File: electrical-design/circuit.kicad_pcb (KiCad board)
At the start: 4 copper layers, 90 x 70 mm, 49 parts, among them J1 AVR-ISP-10, J2 Analoge Header, Q1 2N3906, Q2 2N3906, Q3 2N3906, Q4 2N3906, SW1 Reset Button, SW2 SW_DIP_x04, SW3 Reset Button, U1 ATmega8A-P, U2 LTC-4627JD, U3 NE555P, Y1 16MHz

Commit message: Completed Design For Rev 1.0
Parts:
- removed kibuzzard-63E778F7: G***, kibuzzard-63E778F7
- added C7: 33uF, Capacitor_THT:CP_Radial_D4.0mm_P1.50mm, F.Cu at (129.0, 63.5)
- moved R2 14.7 mm to (122.4, 83.6)
- moved R3 7.78 mm to (122.4, 81.0)
- moved D1 1.27 mm to (136.9, 82.5)
- moved D2 1.27 mm to (128.5, 82.5)
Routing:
- net Net-(D1-K): track 4.57 -> 15.7 mm
- net Net-(D2-K): track 4.58 -> 6.73 mm
- net Net-(D2-A): track 9.27 -> 10.5 mm
- net Net-(D1-A): track 17.8 -> 19.1 mm
- net Net-(U2-DP): track 49.6 -> 49.1 mm
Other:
- board text added: "ATMEGA8A Evaluation Board"
- board text added: "Rev 1.0"

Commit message: Created Parts Order List And Modified PCB Rev 1.0 Accordingly
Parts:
- removed J2: Analoge Header, Connector_JST:JST_XH_B3B-XH-A_1x03_P2.50mm_Vertical
- added TP1: TP Ground, TestPoint:TestPoint_THTPad_2.0x2.0mm_Drill1.0mm, F.Cu at (103.6, 86.4)
- added TP2: TP Frequency, TestPoint:TestPoint_THTPad_2.0x2.0mm_Drill1.0mm, F.Cu at (109.7, 86.4)
- added VR1: PTV09A-4015F-B503, Potentiometer:PTV09A4020FB103, F.Cu at (137.1, 38.6)
- C7: footprint Capacitor_THT:CP_Radial_D4.0mm_P1.50mm -> Capacitor_THT:CP_Radial_D4.0mm_P2.00mm
- SW2: value SW_DIP_x04 -> DS02C-254-1L-04BE; footprint Button_Switch_THT:SW_DIP_SPSTx04_Slide_9.78x12.34mm_W7.62mm_P2.54mm -> DIP Switch:DS02C2541L04BE
- U2: value LTC-4627JD -> LTC-4627JR; footprint Display_7Segment:LTC-4627Jx -> 7 Segment Display:DIPS1016W50P254L4018H725Q16N
- moved R15 18.3 mm to (84.3, 87.4), turned to 180 degrees
- moved R14 15.7 mm to (84.3, 84.8), turned to 180 degrees
- moved R13 13.5 mm to (84.3, 82.3), turned to 180 degrees
- moved R12 12.1 mm to (84.3, 79.8), turned to 180 degrees
- moved SW2 10.8 mm to (66.3, 76.4), turned to 0 degrees
- moved J1 2.02 mm to (136.8, 55.9)
- moved C7 0.22 mm to (128.8, 63.5)
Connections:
- R12 pad 2: Net-(R12-Pad2) -> Net-(SW2-COM4)
- R13 pad 2: Net-(R13-Pad2) -> Net-(SW2-COM3)
- R14 pad 2: Net-(R14-Pad2) -> Net-(SW2-COM2)
- R15 pad 2: Net-(R15-Pad2) -> Net-(SW2-COM1)
- R16 pad 2: Net-(U3-DIS) -> Net-(SW2-NO1)
- R17 pad 1: Net-(U3-DIS) -> Net-(SW2-NO1)
- SW2 pad 1: Net-(U3-DIS) -> Net-(SW2-COM1)
- SW2 pad 2: Net-(U3-DIS) -> Net-(SW2-COM2)
- SW2 pad 3: Net-(U3-DIS) -> Net-(SW2-COM3)
- SW2 pad 4: Net-(U3-DIS) -> Net-(SW2-COM4)
- SW2 pad 5: Net-(R15-Pad2) -> Net-(SW2-NO1)
- SW2 pad 6: Net-(R14-Pad2) -> Net-(SW2-NO1)
- SW2 pad 7: Net-(R13-Pad2) -> Net-(SW2-NO1)
- SW2 pad 8: Net-(R12-Pad2) -> Net-(SW2-NO1)
- U3 pad 7: Net-(U3-DIS) -> Net-(SW2-NO1)
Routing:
- net Net-(U3-DIS): track 35.7 -> 0.00 mm
- net Net-(SW2-NO1): track 0.00 -> 35.7 mm
- net Net-(SW2-COM1): track 0.00 -> 17.5 mm
- net Net-(SW2-COM2): track 0.00 -> 13.9 mm
- net Net-(SW2-COM3): track 0.00 -> 10.3 mm
- net Net-(SW2-COM4): track 0.00 -> 6.73 mm
- net Net-(R15-Pad2): track 4.25 -> 0.00 mm
- net Net-(R14-Pad2): track 4.25 -> 0.00 mm
- net Net-(R13-Pad2): track 4.25 -> 0.00 mm
- net Net-(R12-Pad2): track 4.25 -> 0.00 mm
- net Net-(U1-PC4): track 16.7 -> 20.3 mm
- net Frequency: track 42.9 -> 46.1 mm
- net ~{RESET}: track 43.5 -> 46.3 mm
- net MISO: track 13.3 -> 12.4 mm
- net SCK: track 13.3 -> 12.4 mm

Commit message: Send R1.0 to Production
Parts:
- added R24: 1K, Resistor_THT:R_Axial_DIN0204_L3.6mm_D1.6mm_P5.08mm_Horizontal, F.Cu at (128.3, 47.8)
- added R25: 1K, Resistor_THT:R_Axial_DIN0204_L3.6mm_D1.6mm_P5.08mm_Horizontal, F.Cu at (128.3, 29.5)
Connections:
- VR1 pad 1: VCC -> Net-(R24-Pad2)
- VR1 pad 3: GND -> Net-(R25-Pad2)
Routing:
- net Net-(R24-Pad2): track 0.00 -> 13.0 mm
- net Net-(R25-Pad2): track 0.00 -> 13.0 mm
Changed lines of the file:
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@@
   (net 58 "Net-(SW2-COM3)")
   (net 59 "Net-(SW2-COM4)")
+  (net 60 "Net-(R25-Pad2)")
+  (net 61 "Net-(R24-Pad2)")
   (footprint "Button_Switch_THT:SW_PUSH_6mm_H5mm" (layer "F.Cu")
     (at 88.19 81.062)
@@
     )
   )
+  (footprint "Resistor_THT:R_Axial_DIN0204_L3.6mm_D1.6mm_P5.08mm_Horizontal" (layer "F.Cu")
+    (at 128.27 29.464)
+    (descr "Resistor, Axial_DIN0204 series, Axial, Horizontal, pin pitch=5.08mm, 0.167W, length*diameter=3.6*1.6mm^2, http://cdn-reichelt.de/documents/datenblatt/B400/1_4W%23YAG.pdf")
+    (tags "Resistor Axial_DIN0204 series Axial Horizontal pin pitch 5.08mm 0.167W length 3.6mm diameter 1.6mm")
+    (property "Sheetfile" "circuit.kicad_sch")
+    (property "Sheetname" "")
+    (property "ki_description" "Resistor, small symbol")
+    (property "ki_keywords" "R resistor")
+    (attr through_hole)
+    (fp_text reference "R25" (at 2.54 -1.92) (layer "F.SilkS")
+        (effects (font (size 0.75 0.75) (thickness 0.1)))
+    )
+    (fp_text value "1K" (at 2.54 1.92 unlocked) (layer "F.Fab")
+        (effects (font (size 1 1) (thickness 0.15)))
+    )
+    (fp_text user "${REFERENCE}" (at 2.54 0 unlocked) (layer "F.Fab")
+        (effects (font (size 1 1) (thickness 0.15)))
+    )
+    (fp_line (start 0.62 -0.92) (end 4.46 -0.92)
+      (stroke (width 0.1) (type solid)) (layer "F.SilkS"))
+    (fp_line (start 0.62 0.92) (end 4.46 0.92)
+      (stroke (width 0.1) (type solid)) (layer "F.SilkS"))
+    (fp_line (start -0.95 -1.05) (end -0.95 1.05)
+      (stroke (width 0.05) (type solid)) (layer "F.CrtYd"))
+    (fp_line (start -0.95 1.05) (end 6.03 1.05)
+      (stroke (width 0.05) (type solid)) (layer "F.CrtYd"))
+    (fp_line (start 6.03 -1.05) (end -0.95 -1.05)
+      (stroke (width 0.05) (type solid)) (layer "F.CrtYd"))
+    (fp_line (start 6.03 1.05) (end 6.03 -1.05)
+      (stroke (width 0.05) (type solid)) (layer "F.CrtYd"))
+    (fp_line (start 0 0) (end 0.74 0)
+      (stroke (width 0.1) (type solid)) (layer "F.Fab"))
+    (fp_line (start 0.74 -0.8) (end 0.74 0.8)
+      (stroke (width 0.1) (type solid)) (layer "F.Fab"))
+    (fp_line (start 0.74 0.8) (end 4.34 0.8)
+      (stroke (width 0.1) (type solid)) (layer "F.Fab"))
+    (fp_line (start 4.34 -0.8) (end 0.74 -0.8)
+      (stroke (width 0.1) (type solid)) (layer "F.Fab"))
+    (fp_line (start 4.34 0.8) (end 4.34 -0.8)
+      (stroke (width 0.1) (type solid)) (layer "F.Fab"))
+    (fp_line (start 5.08 0) (end 4.34 0)
+      (stroke (width 0.1) (type solid)) (layer "F.Fab"))
+    (pad "1" thru_hole circle (at 0 0) (size 1.4 1.4) (drill 0.7) (layers "*.Cu" "*.Mask")
+      (net 13 "GND") (pintype "passive"))
+    (pad "2" thru_hole oval (at 5.08 0) (size 1.4 1.4) (drill 0.7) (layers "*.Cu" "*.Mask")
+      (net 60 "Net-(R25-Pad2)") (pintype "passive"))
+    (model "${KICAD6_3DMODEL_DIR}/Resistor_THT.3dshapes/R_Axial_DIN0204_L3.6mm_D1.6mm_P5.08mm_Horizontal.wrl"
+      (offset (xyz 0 0 0))
+      (scale (xyz 1 1 1))
+      (rotate (xyz 0 0 0))
+    )
+  )
   (footprint "MountingHole:MountingHole_2.2mm_M2_DIN965_Pad_TopBottom" (layer "F.Cu")
     (at 142.96 27.94)
@@
   )
   (footprint "Resistor_THT:R_Axial_DIN0204_L3.6mm_D1.6mm_P5.08mm_Horizontal" (layer "F.Cu")
+    (at 128.27 47.752)
+    (descr "Resistor, Axial_DIN0204 series, Axial, Horizontal, pin pitch=5.08mm, 0.167W, length*diameter=3.6*1.6mm^2, http://cdn-reichelt.de/documents/datenblatt/B400/1_4W%23YAG.pdf")
+    (tags "Resistor Axial_DIN0204 series Axial Horizontal pin pitch 5.08mm 0.167W length 3.6mm diameter 1.6mm")
+    (property "Sheetfile" "circuit.kicad_sch")
+    (property "Sheetname" "")
+    (property "ki_description" "Resistor, small symbol")
+    (property "ki_keywords" "R resistor")
+    (attr through_hole)
+    (fp_text reference "R24" (at 2.54 -1.92) (layer "F.SilkS")
+        (effects (font (size 0.75 0.75) (thickness 0.1)))
+    )
+    (fp_text value "1K" (at 2.54 1.92 180 unlocked) (layer "F.Fab")
+        (effects (font (size 1 1) (thickness 0.15)))
+    )
+    (fp_text user "${REFERENCE}" (at 2.54 0 180 unlocked) (layer "F.Fab")
+        (effects (font (size 1 1) (thickness 0.15)))
+    )
+    (fp_line (start 0.62 -0.92) (end 4.46 -0.92)
+      (stroke (width 0.1) (type solid)) (layer "F.SilkS"))
+    (fp_line (start 0.62 0.92) (end 4.46 0.92)
+      (stroke (width 0.1) (type solid)) (layer "F.SilkS"))
+    (fp_line (start -0.95 -1.05) (end -0.95 1.05)
+      (stroke (width 0.05) (type solid)) (layer "F.CrtYd"))
+    (fp_line (start -0.95 1.05) (end 6.03 1.05)
+      (stroke (width 0.05) (type solid)) (layer "F.CrtYd"))
+    (fp_line (start 6.03 -1.05) (end -0.95 -1.05)
+      (stroke (width 0.05) (type solid)) (layer "F.CrtYd"))
+    (fp_line (start 6.03 1.05) (end 6.03 -1.05)
+      (stroke (width 0.05) (type solid)) (layer "F.CrtYd"))
+    (fp_line (start 0 0) (end 0.74 0)
+      (stroke (width 0.1) (type solid)) (layer "F.Fab"))
+    (fp_line (start 0.74 -0.8) (end 0.74 0.8)
+      (stroke (width 0.1) (type solid)) (layer "F.Fab"))
+    (fp_line (start 0.74 0.8) (end 4.34 0.8)
+      (stroke (width 0.1) (type solid)) (layer "F.Fab"))
+    (fp_line (start 4.34 -0.8) (end 0.74 -0.8)
+      (stroke (width 0.1) (type solid)) (layer "F.Fab"))
+    (fp_line (start 4.34 0.8) (end 4.34 -0.8)
+      (stroke (width 0.1) (type solid)) (layer "F.Fab"))
+    (fp_line (start 5.08 0) (end 4.34 0)
+      (stroke (width 0.1) (type solid)) (layer "F.Fab"))
+    (pad "1" thru_hole circle (at 0 0) (size 1.4 1.4) (drill 0.7) (layers "*.Cu" "*.Mask")
+      (net 1 "VCC") (pintype "passive"))
+    (pad "2" thru_hole oval (at 5.08 0) (size 1.4 1.4) (drill 0.7) (layers "*.Cu" "*.Mask")
+      (net 61 "Net-(R24-Pad2)") (pintype "passive"))
+    (model "${KICAD6_3DMODEL_DIR}/Resistor_THT.3dshapes/R_Axial_DIN0204_L3.6mm_D1.6mm_P5.08mm_Horizontal.wrl"
+      (offset (xyz 0 0 0))
+      (scale (xyz 1 1 1))
+      (rotate (xyz 0 0 0))
+    )
+  )
+  (footprint "Resistor_THT:R_Axial_DIN0204_L3.6mm_D1.6mm_P5.08mm_Horizontal" (layer "F.Cu")
     (at 84.328 84.836 180)
     (descr "Resistor, Axial_DIN0204 series, Axial, Horizontal, pin pitch=5.08mm, 0.167W, length*diameter=3.6*1.6mm^2, http://cdn-reichelt.de/documents/datenblatt/B400/1_4W%23YAG.pdf")
@@
       (stroke (width 0.1) (type solid)) (layer "F.Fab"))
     (pad "1" thru_hole circle (at -2.5 5.6 90) (size 1.8 1.8) (drill 1.2) (layers "*.Cu" "*.Mask")
-      (net 1 "VCC") (pinfunction "1") (pintype "passive"))
+      (net 61 "Net-(R24-Pad2)") (pinfunction "1") (pintype "passive"))
     (pad "2" thru_hole circle (at 0 5.6 90) (size 1.8 1.8) (drill 1.2) (layers "*.Cu" "*.Mask")
       (net 40 "Net-(U1-PC4)") (pinfunction "2") (pintype "passive"))
     (pad "3" thru_hole circle (at 2.5 5.6 90) (size 1.8 1.8) (drill 1.2) (layers "*.Cu" "*.Mask")
-      (net 13 "GND") (pinfunction "3") (pintype "passive"))
+      (net 60 "Net-(R25-Pad2)") (pinfunction "3") (pintype "passive"))
     (pad "4" thru_hole circle (at -4.4 -1.4 90) (size 4.46 4.46) (drill 2.9732) (layers "*.Cu" "*.Mask")
       (net 41 "unconnected-(VR1-Pad4)") (pinfunction "4") (pintype "passive+no_connect"))
@@
   (segment (start 77.275 79.756) (end 73.914 76.395) (width 0.2) (layer "In1.Cu") (net 59))
   (segment (start 79.248 79.756) (end 77.275 79.756) (width 0.2) (layer "In1.Cu") (net 59))
+  (segment (start 142.748 34.798) (end 137.414 29.464) (width 0.2) (layer "In1.Cu") (net 60))
+  (segment (start 142.748 36.148) (end 142.748 34.798) (width 0.2) (layer "In1.Cu") (net 60))
+  (segment (start 137.414 29.464) (end 133.35 29.464) (width 0.2) (layer "In1.Cu") (net 60))
+  (segment (start 137.668 47.752) (end 133.35 47.752) (width 0.2) (layer "In1.Cu") (net 61))
+  (segment (start 142.748 41.148) (end 142.748 42.672) (width 0.2) (layer "In1.Cu") (net 61))
+  (segment (start 142.748 42.672) (end 137.668 47.752) (width 0.2) (layer "In1.Cu") (net 61))
   (zone locked (net 1) (net_name "VCC") (layer "F.Cu") (hatch edge 0.508)
     (connect_pads (clearance 0.508))

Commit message: Started Design For Rev 1.1
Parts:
- added C2: 0.1uF, Capacitor_THT:C_Disc_D3.0mm_W2.0mm_P2.50mm, F.Cu at (110.1, 37.2)
- added R1: 330, Resistor_THT:R_Axial_DIN0204_L3.6mm_D1.6mm_P5.08mm_Horizontal, F.Cu at (107.6, 34.3)
- SW1: footprint Button_Switch_THT:SW_PUSH_6mm_H5mm -> Button_Switch_THT:SW_PUSH_6mm
- moved C7 1.26 mm to (97.3, 78.7)
- moved C8 1.26 mm to (97.3, 67.1)
- moved R12 1.26 mm to (83.1, 87.4)
- moved R13 1.26 mm to (83.1, 84.8)
- moved R14 1.26 mm to (83.1, 82.3)
- moved R15 1.26 mm to (83.1, 79.8)
- moved R16 1.26 mm to (78.0, 71.1)
- moved R17 1.26 mm to (97.3, 69.8)
- moved R22 1.26 mm to (78.0, 73.7)
- moved R24 1.26 mm to (78.0, 76.2)
- moved SW2 1.26 mm to (65.0, 76.4)
- moved SW3 1.26 mm to (86.9, 81.1)
- moved U3 1.26 mm to (86.4, 68.6)
- moved R10 0.76 mm to (129.0, 29.5)
- moved R9 0.76 mm to (129.0, 47.8)
- renumbered C7 to C1, C1 to C3, C2 to C4, C3 to C5, C4 to C7, C5 to C8, H4 to H1, H1 to H2, H2 to H4, R25 to R10, R3 to R11, R15 to R12, R14 to R13, R13 to R14, R12 to R15, R7 to R18, R8 to R19, R1 to R2, R11 to R20, R19 to R21, R18 to R22, R20 to R23, R21 to R24, R22 to R25, R23 to R26, R5 to R3, R10 to R4, R4 to R5, R9 to R7, R2 to R8, R24 to R9, TP2 to TP1, TP1 to TP2
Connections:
- SW1 pad 2: ~{RESET} -> Net-(R1-Pad2)
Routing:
- net Net-(R1-Pad2): track 0.00 -> 13.0 mm
- net ~{RESET}: track 46.3 -> 54.6 mm
- net Frequency: track 46.1 -> 47.3 mm
- net Net-(R9-Pad2): track 13.0 -> 12.3 mm
- net Net-(R10-Pad2): track 13.0 -> 12.2 mm
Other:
- board text added: "Rev 1.1"
- board text removed: "Rev 1.0"

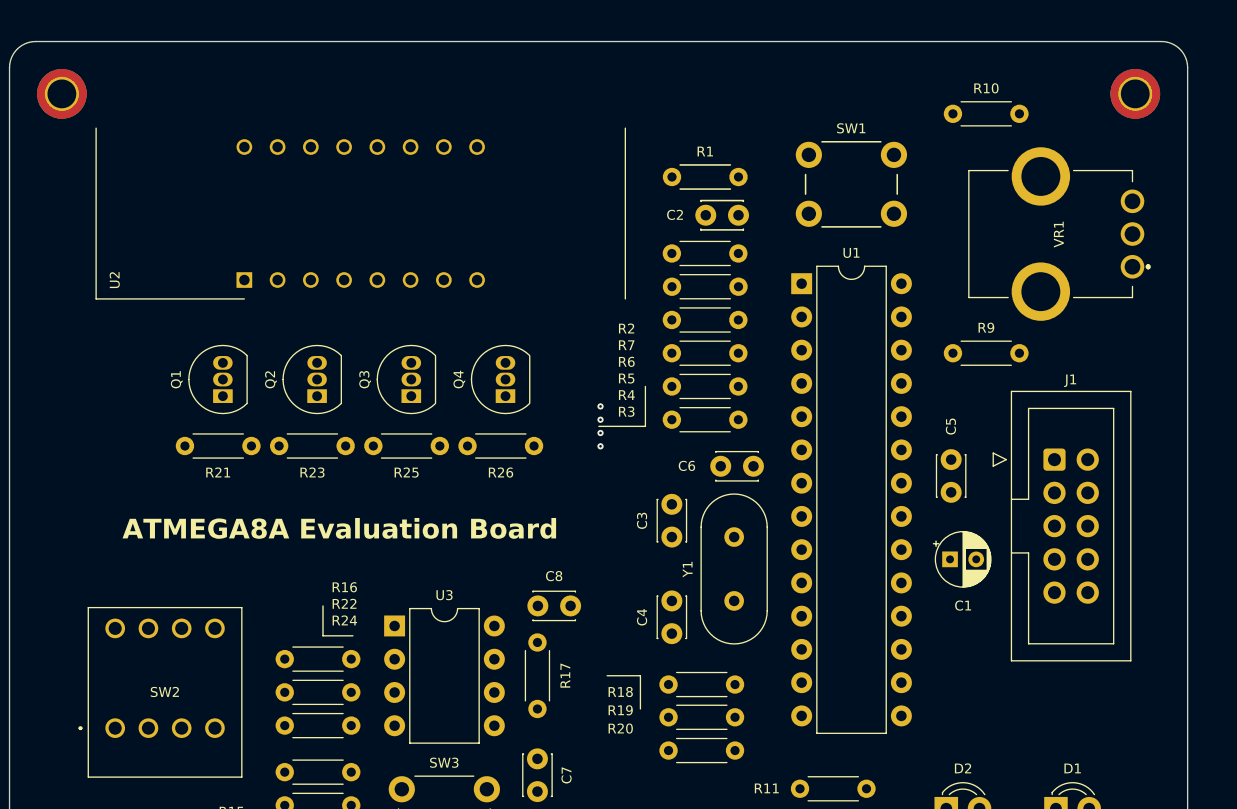
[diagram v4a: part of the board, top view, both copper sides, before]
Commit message: Changed ISP-10 Footprint to ISP-6
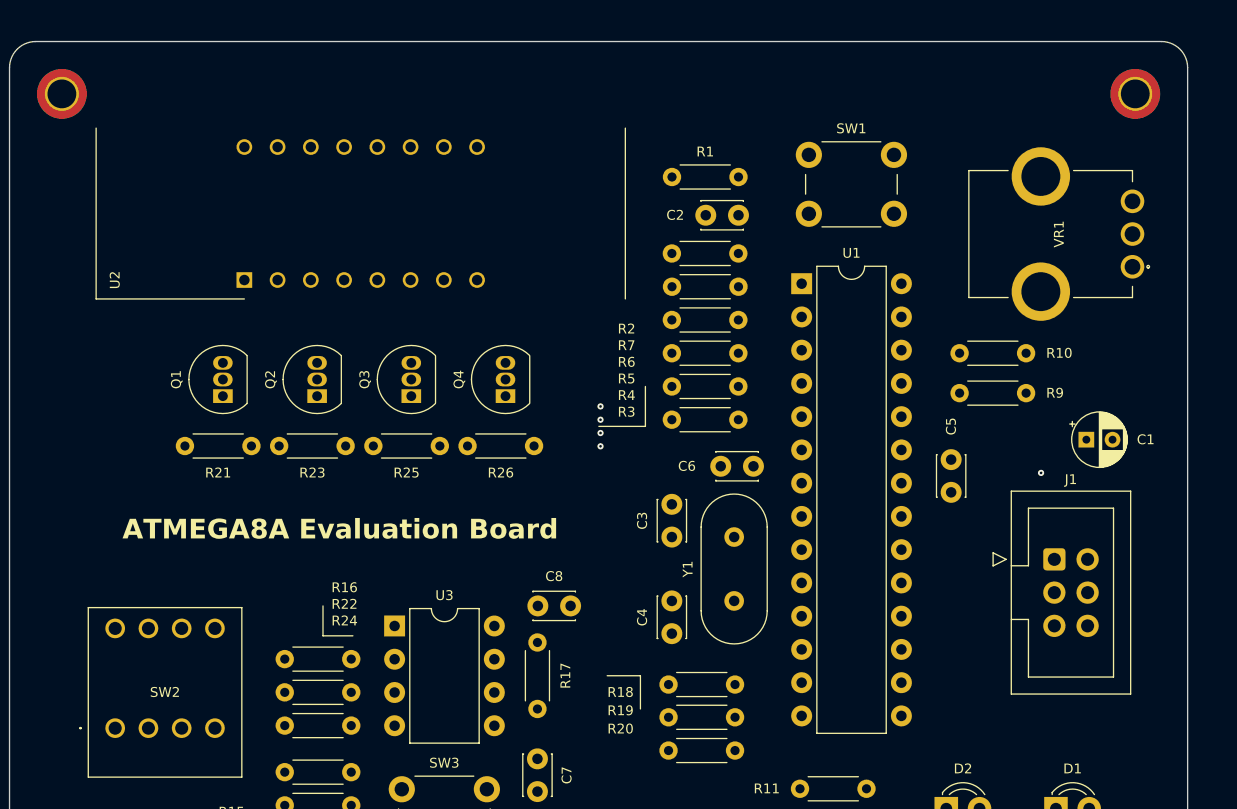
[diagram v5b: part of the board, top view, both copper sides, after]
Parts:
- J1: value AVR-ISP-10 -> AVR-ISP-6; footprint Connector_IDC:IDC-Header_2x05_P2.54mm_Vertical -> Connector_IDC:IDC-Header_2x03_P2.54mm_Vertical
- moved R10 18.3 mm to (129.5, 47.8)
- moved C1 13.9 mm to (139.2, 54.4)
- moved J1 7.62 mm to (136.8, 63.5)
- moved R9 3.09 mm to (129.5, 50.8)
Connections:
- J1 pad 1: MOSI -> MISO
- J1 pad 3: unconnected-(J1-NC-Pad3) -> SCK
- J1 pad 4: GND -> MOSI
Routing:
- net MOSI: track 27.0 -> 16.0 mm
- net ~{RESET}: track 54.6 -> 62.6 mm, vias 0 -> 1
- net Net-(R10-Pad2): track 12.2 -> 15.9 mm
- net Net-(R9-Pad2): track 12.3 -> 13.9 mm
- net MISO: track 12.4 -> 13.5 mm
